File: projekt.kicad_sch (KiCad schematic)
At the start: 84 parts, among them IC1 DW01+G, J11 AO1, J12 BO2, J13 BO1, J14 BO1, J2 TP4056, J3 Conn_01x04_Pin, J4 Conn_01x02_Socket, J5 AO1, J6 USB_C_Receptacle_PowerOnly_6P, J7 AO2, J8 AO2, J9 BO2, Q1 AO3400A, Q2 AO3400A, Q3 AO3400A, Q4 AO3400A, Q5 AO3400A, Q6 AO3400A, SW1 SW_Slide_DPDT, SW2 RST, SW3 BOOT, U2 ESP32-WROOM-32E, U4 TB6612FNG, U7 AMS1117-3.3

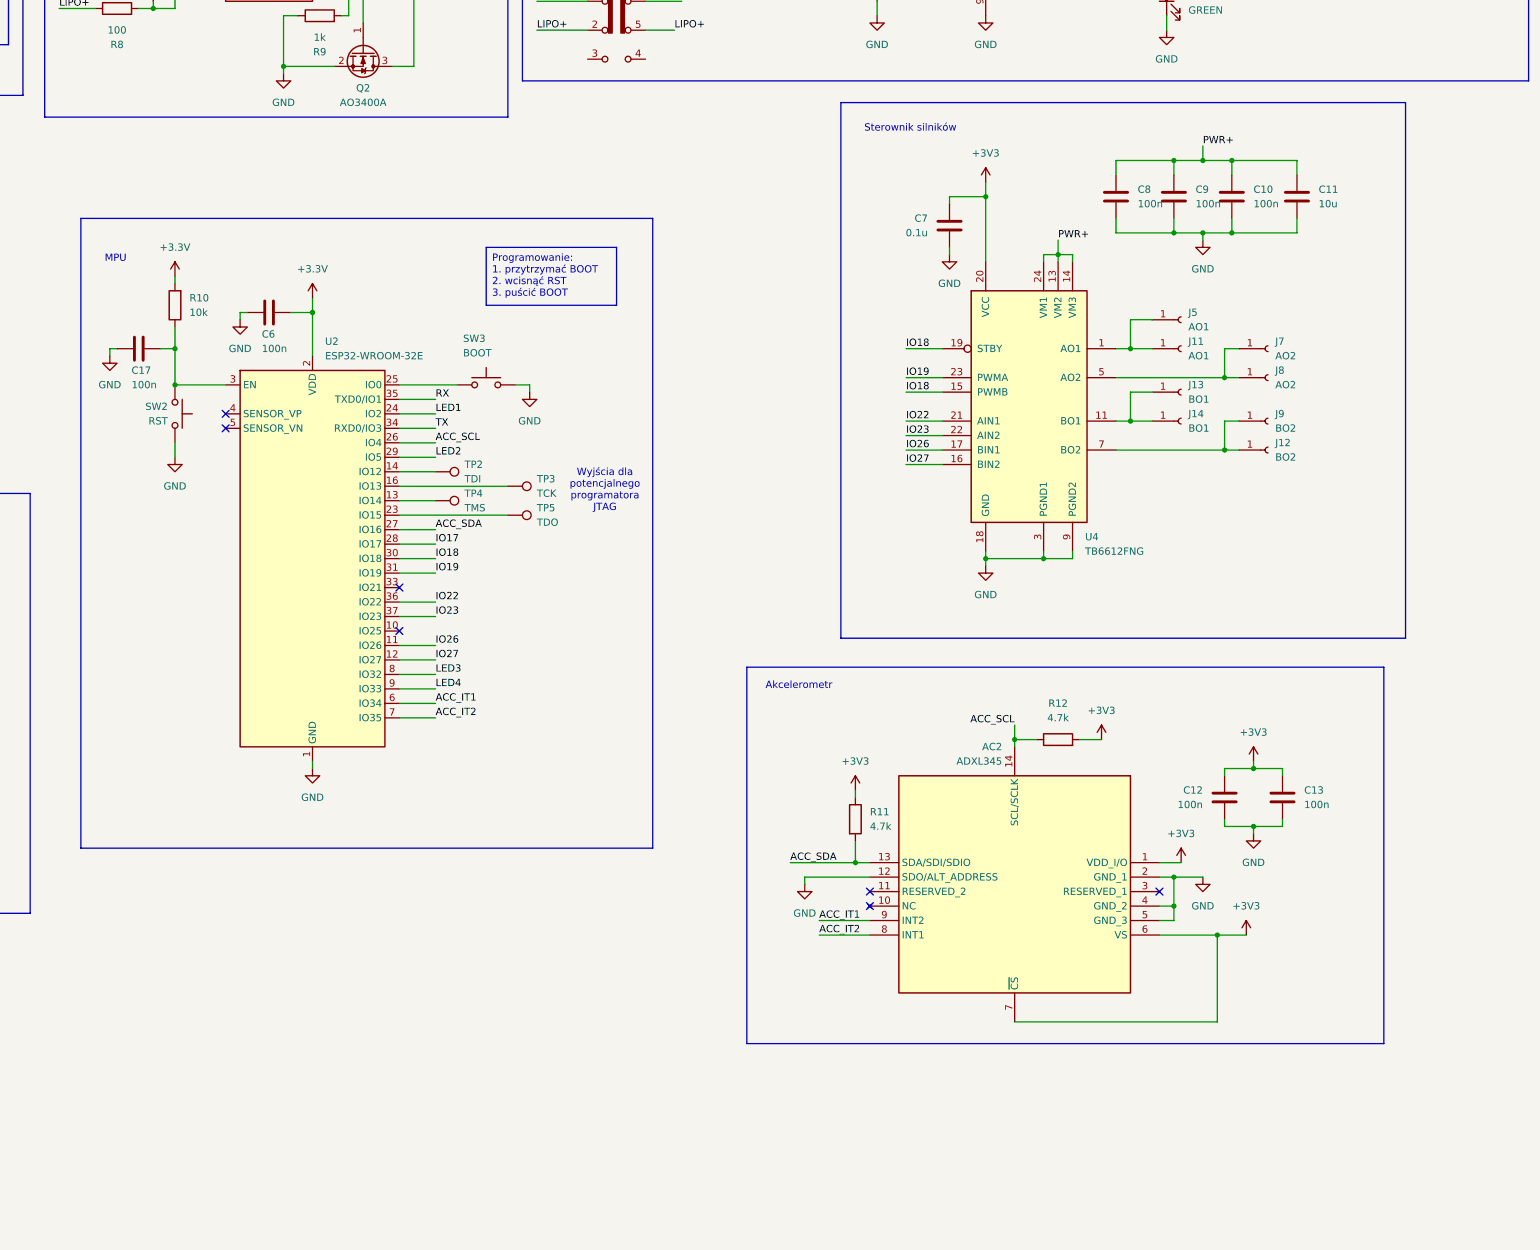
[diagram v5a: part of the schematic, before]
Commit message: Dodanie drugiego DC IC
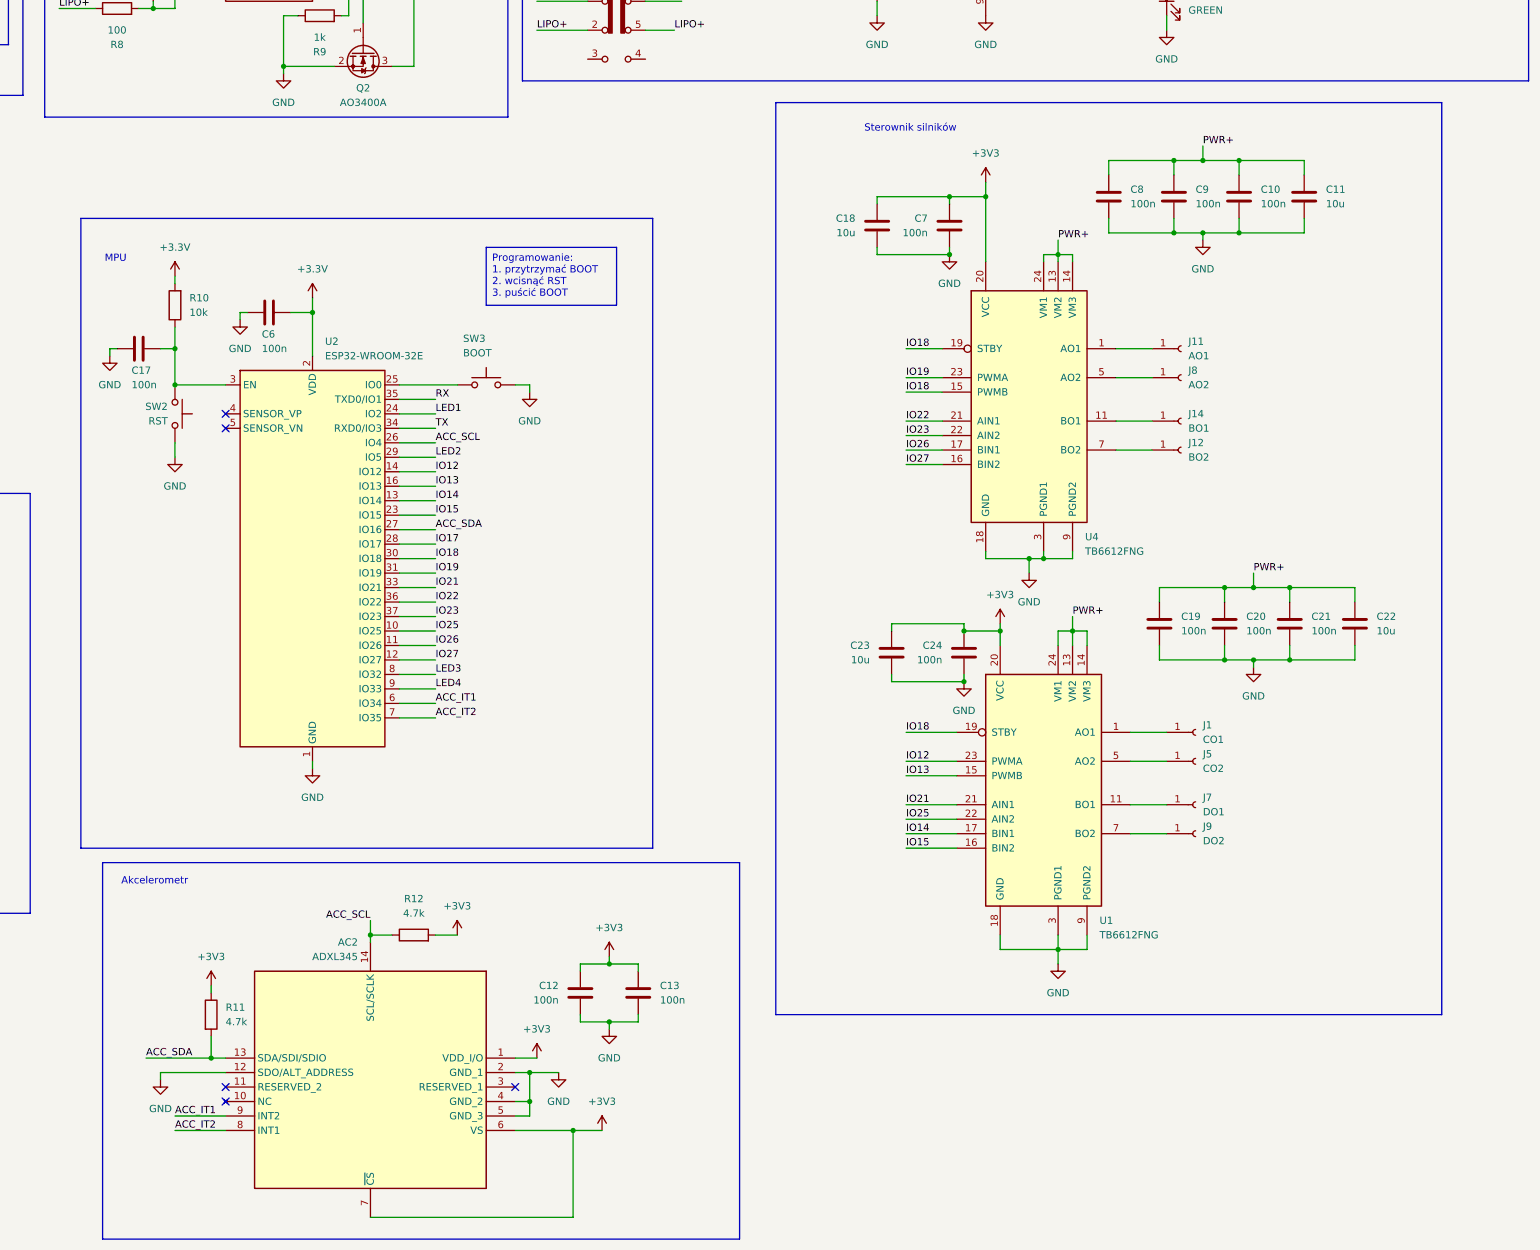
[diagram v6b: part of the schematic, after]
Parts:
- removed J13: BO1, TestPoint:TestPoint_Pad_2.0x2.0mm, symbol Connector:Conn_01x01_Socket
- removed TP2: TDI, TestPoint:TestPoint_Pad_2.0x2.0mm, symbol Connector:TestPoint
- removed TP3: TCK, TestPoint:TestPoint_Pad_2.0x2.0mm, symbol Connector:TestPoint
- removed TP4: TMS, TestPoint:TestPoint_Pad_2.0x2.0mm, symbol Connector:TestPoint
- removed TP5: TDO, TestPoint:TestPoint_Pad_2.0x2.0mm, symbol Connector:TestPoint
- added C18, C22, C23: 10u, Capacitor_SMD:C_0603_1608Metric_Pad1.08x0.95mm_HandSolder, symbol Device:C
- added C19, C20, C21, C24: 100n, Capacitor_SMD:C_0603_1608Metric_Pad1.08x0.95mm_HandSolder, symbol Device:C
- added J1: CO1, TestPoint:TestPoint_Pad_2.0x2.0mm, symbol Connector:Conn_01x01_Socket
- added U1: TB6612FNG, Package_SO:SSOP-24_5.3x8.2mm_P0.65mm, symbol Driver_Motor:TB6612FNG
- C7: value 0.1u -> 100n
- J5: value AO1 -> CO2
- J7: value AO2 -> DO1
- J9: value BO2 -> DO2
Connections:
- net +3V3: now also C18.1, C23.1, C24.1, U1.20 (VCC)
- net GND: now also C18.2, C19.2, C20.2, C21.2, C22.2, C23.2, C24.2, U1.10 (PGND2), U1.18 (GND), U1.3 (PGND1), U1.4 (PGND1), U1.9 (PGND2)
- net IO18: now also U1.19 (STBY)
- net PWR+: now also C19.1, C20.1, C21.1, C22.1, U1.13 (VM2), U1.14 (VM3), U1.24 (VM1)
- net at J11.1 (Pin_1), U4.1 (AO1), U4.2 (AO1): no longer J5.1 (Pin_1)
- net IO25: now reaches U2.10 (IO25)
- net IO25: now also U1.22 (AIN2)
- net IO14: now reaches U2.13 (IO14)
- net IO14: now also U1.17 (BIN1)
- net IO12: now reaches U2.14 (IO12)
- net IO12: now also U1.23 (PWMA)
- net IO13: now reaches U2.16 (IO13)
- net IO13: now also U1.15 (PWMB)
- net IO15: now reaches U2.23 (IO15)
- net IO15: now also U1.16 (BIN2)
- net IO21: now reaches U2.33 (IO21)
- net IO21: now also U1.21 (AIN1)
- net at J12.1 (Pin_1), U4.7 (BO2), U4.8 (BO2): no longer J9.1 (Pin_1)
- net at J8.1 (Pin_1), U4.5 (AO2), U4.6 (AO2): no longer J7.1 (Pin_1)
- new net: J1.1 (Pin_1), U1.1 (AO1), U1.2 (AO1)
- new net: J7.1 (Pin_1), U1.11 (BO1), U1.12 (BO1)
- new net: J5.1 (Pin_1), U1.5 (AO2), U1.6 (AO2)
- new net: J9.1 (Pin_1), U1.7 (BO2), U1.8 (BO2)
- no-connect marks 8 -> 6
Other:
- note removed: "Wyjścia dla potencjalnego programatora JTAG"
- moved on the sheet: AC2, C10, C11, C12, C13, C8, J12, J8, R11, R12

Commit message: Praca nad PCB
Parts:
- removed J3: Conn_01x04_Pin, Connector_PinHeader_2.54mm:PinHeader_1x04_P2.54mm_Vertical, symbol Connector:Conn_01x04_Pin
- removed J6: USB_C_Receptacle_PowerOnly_6P, Connector_USB:USB_C_Receptacle_GCT_USB4125-xx-x-0190_6P_TopMnt_Horizontal, symbol Connector:USB_C_Receptacle_PowerOnly_6P
- added C25: 100n, Capacitor_SMD:C_0603_1608Metric_Pad1.08x0.95mm_HandSolder, symbol Device:C
- added IC2, IC3: SS8050-HF, SOT95P240X115-3N, symbol SamacSys_Parts:SS8050-HF
- added J10: Conn_01x06_Pin, Connector_PinHeader_2.54mm:PinHeader_1x06_P2.54mm_Vertical, symbol Connector:Conn_01x06_Pin
- added J6: USB_C_Receptacle_PowerOnly_24P, Connector_USB:USB_C_Receptacle_GCT_USB4110, symbol Connector:USB_C_Receptacle_PowerOnly_24P
- added R28, R29, R30, R31: 10k, Resistor_SMD:R_0603_1608Metric_Pad0.98x0.95mm_HandSolder, symbol Device:R
- R8: value 100 -> 10k
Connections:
- net +3.3V: now also J10.1 (Pin_1), R29.2, R31.2
- net GND: now also R8.1, C25.1, J10.6 (Pin_6), J6.A1 (GND), J6.A12 (GND), J6.B1 (GND), J6.B12 (GND), J6.S1 (SHIELD), R30.1; no longer R15.1, SW3.1
- net IO12: now also R30.2
- net IO15: now also R29.1
- net LED2: now also R31.1; no longer R15.2
- net LIPO+: now also C5.2, IC1.5 (VCC); no longer R8.1
- net RX: now also J10.2 (Pin_2)
- net TX: now also J10.3 (Pin_3)
- net VCC: now also J6.A4 (VBUS), J6.A9 (VBUS), J6.B4 (VBUS), J6.B9 (VBUS)
- net BOOT: now reaches SW3.2, U2.25 (IO0)
- net BOOT: now also C25.2, IC3.3 (C)
- net EN: now reaches C17.1, R10.1, SW2.2, U2.3 (EN)
- net EN: now also IC2.3 (C)
- net at R2.1: now also J6.A5 (CC1)
- net at R1.1: now also J6.B5 (CC2)
- new net: IC3.1 (B), R28.1
- new net: R8.2, SW3.1
- new net: IC2.1 (B), R15.1
- new net DTR: IC3.2 (E), J10.4 (Pin_4), R15.2
- new net RTS: IC2.2 (E), J10.5 (Pin_5), R28.2
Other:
- note added: "Automatyczne ustawienie EN i BOOT przez programator"
- note added: "GPIO2 Już ma pulldown"
- note added: "Pull-Upy/Pull-downy potrzebne do bootowania"
- note added: "Wcześniej jest pullup, dlatego nie ma pulldown"
- moved on the sheet: C17, C6, D4, D5, D6, D7, Q3, Q4, Q5, Q6, R10, R13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

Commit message: wstępne ułożenie elementów
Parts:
- SW2, SW3: footprint Button_Switch_SMD:SW_Push_1P1T_NO_CK_KSC7xxJ -> Button_Switch_SMD:SW_SPST_B3U-1000P
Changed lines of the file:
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@@
 			)
 		)
-		(property "Footprint" "Button_Switch_SMD:SW_Push_1P1T_NO_CK_KSC7xxJ"
+		(property "Footprint" "Button_Switch_SMD:SW_SPST_B3U-1000P"
 			(at 157.48 160.02 0)
 			(effects
@@
 			)
 		)
-		(property "Footprint" "Button_Switch_SMD:SW_Push_1P1T_NO_CK_KSC7xxJ"
+		(property "Footprint" "Button_Switch_SMD:SW_SPST_B3U-1000P"
 			(at 247.65 119.38 0)
 			(effects
